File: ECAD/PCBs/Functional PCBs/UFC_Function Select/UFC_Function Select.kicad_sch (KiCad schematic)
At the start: 15 parts

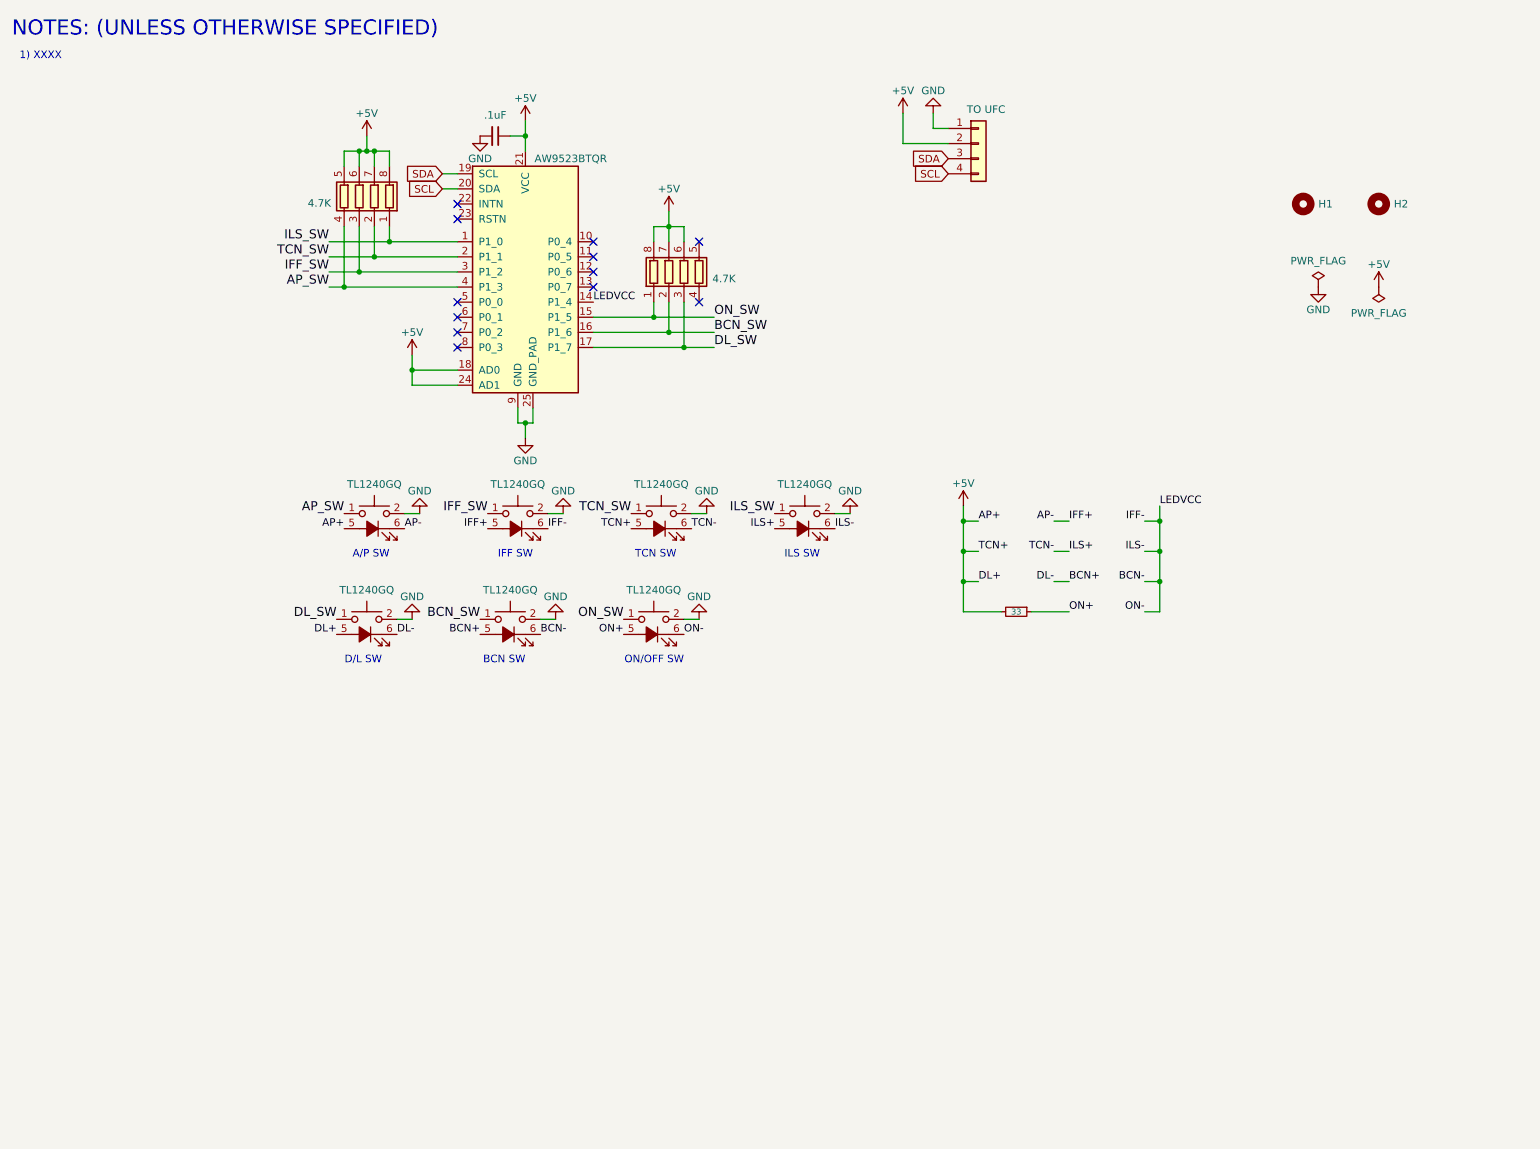
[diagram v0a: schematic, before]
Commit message: ECAD Update
Throttle Controller
-Simplified the solenoid relay circuits
-changed to S2-MINI microcontroller
-Added a second AUX I2C for future ATC connection
-Same mechanical footprint.
UFC v5.5 MAIN and AP KB files (didn't make it last time, oops.)
Added pin sockets 3d model to S2 Mini footprint
Added S2 Mini footprint to the symbol.
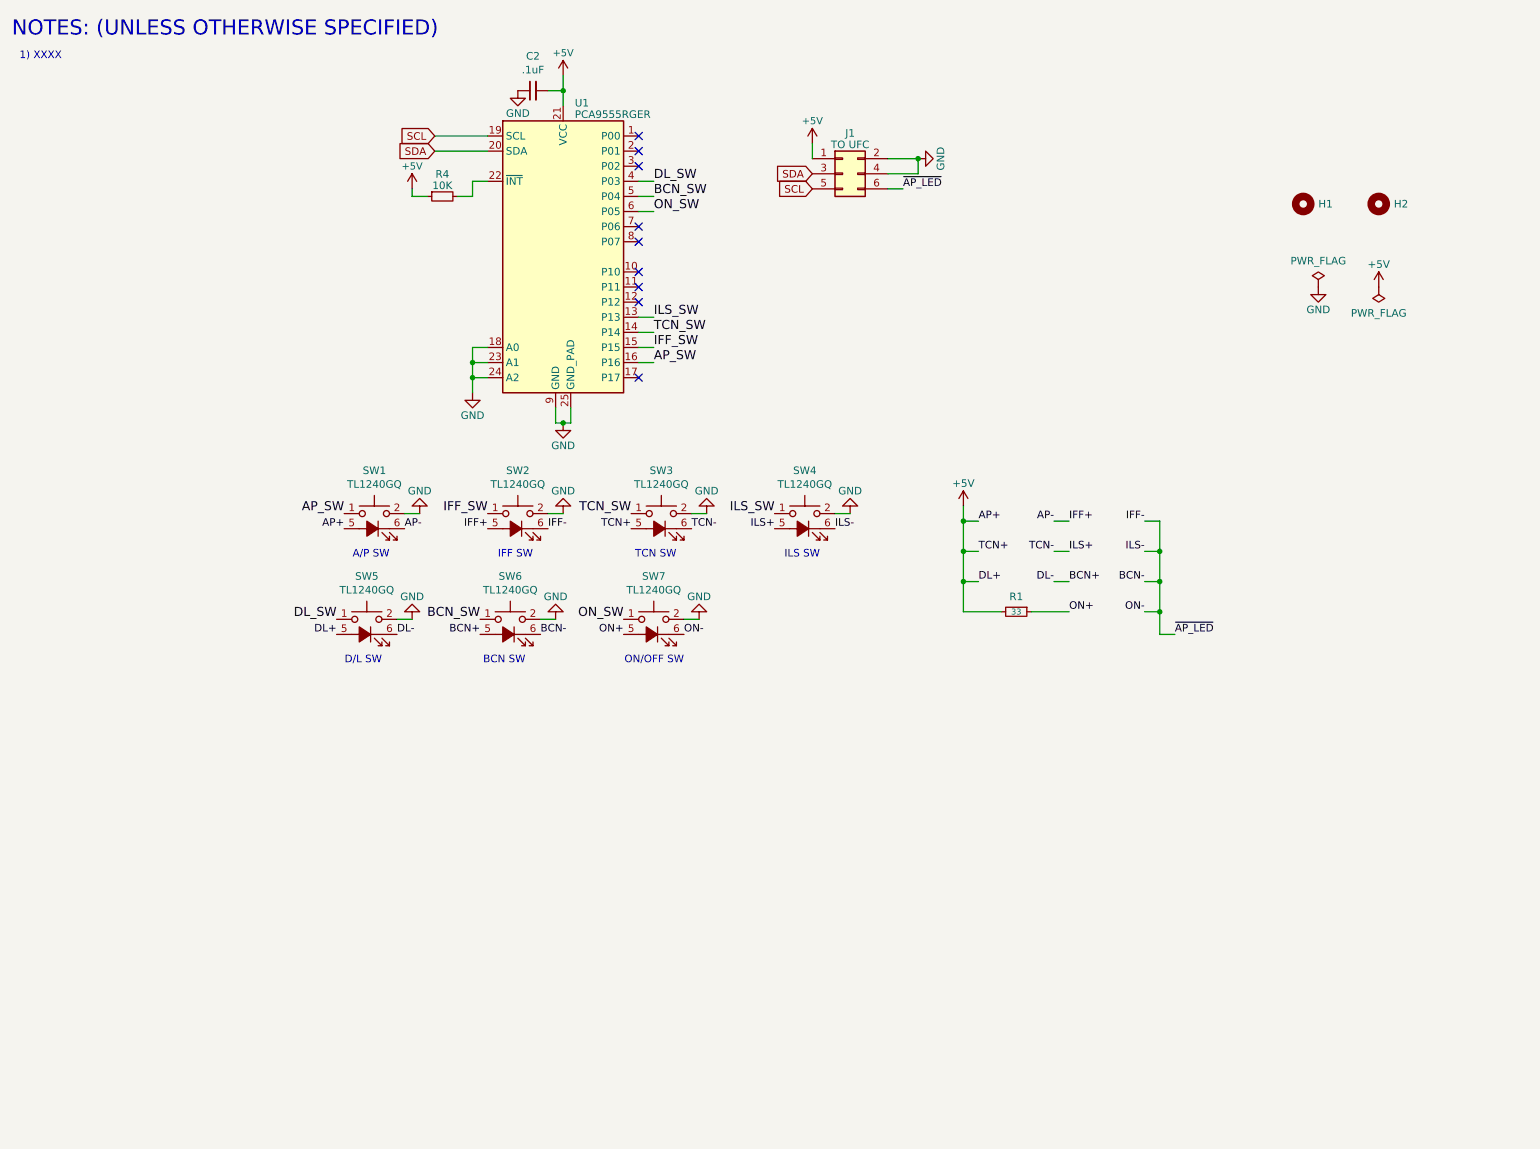
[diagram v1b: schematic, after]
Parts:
- removed ?: TO UFC, Connector_PinHeader_2.54mm:PinHeader_1x04_P2.54mm_Vertical, symbol Connector_Generic:Conn_01x04
- removed ?: AW9523BTQR, Package_DFN_QFN:WQFN-24-1EP_4x4mm_P0.5mm_EP2.6x2.6mm, symbol UFC_Function-Select-rescue:AW9523BTQR-KiCadCustomLib
- removed ?: .1uF, Capacitor_SMD:C_0603_1608Metric, symbol Device:C_Small
- removed ? (x2): 4.7K, Resistor_SMD:R_Array_Convex_4x0603, symbol Device:R_Pack04
- added C2: .1uF, Capacitor_SMD:C_0603_1608Metric, symbol Device:C_Small
- added J1: TO UFC, Connector_PinHeader_2.54mm:PinHeader_2x03_P2.54mm_Vertical, symbol Connector_Generic:Conn_02x03_Odd_Even
- added R4: 10K, Resistor_SMD:R_0603_1608Metric, symbol Device:R_Small
- added U1: PCA9555RGER, Package_DFN_QFN:VQFN-24-1EP_4x4mm_P0.5mm_EP2.45x2.45mm, symbol KiCadCustomLib:PCA9555RGER
- SW1, SW2, SW3, SW4, SW5, SW6, SW7: renamed from ?; footprint KiCAD_Libraries:TL1240GQ -> OH_Footprints:TL1240GQ; symbol UFC_Function-Select-rescue:TL1240GQ-KiCadCustomLib -> KiCadCustomLib:TL1240GQ
- gave numbers to parts that had none: 1
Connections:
- net +5V: now also C2.2, J1.1 (Pin_1), R4.1, U1.21 (VCC)
- net AP_SW: now also U1.16 (P16)
- net BCN-: now also J1.6 (Pin_6)
- net BCN_SW: now also U1.5 (P04)
- net DL_SW: now also U1.4 (P03)
- net GND: now also C2.1, J1.2 (Pin_2), J1.4 (Pin_4), U1.18 (A0), U1.23 (A1), U1.24 (A2), U1.25 (GND_PAD), U1.9 (GND)
- net IFF_SW: now also U1.15 (P15)
- net ILS_SW: now also U1.13 (P13)
- net ON_SW: now also U1.6 (P05)
- net SCL: now also J1.5 (Pin_5), U1.19 (SCL)
- net SDA: now also J1.3 (Pin_3), U1.20 (SDA)
- net TCN_SW: now also U1.14 (P14)
- new net: R4.2, U1.22 (~{INT})
- no-connect marks 12 -> 9

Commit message: Updated Function Select PCB
Replaced tactiles with Omron High-Force Tactiles
Added WS2812B-2020s for Backlighting
Added Interrupt (IRQ) line, replacing the center ground pin on the connector.
Ready for test order.
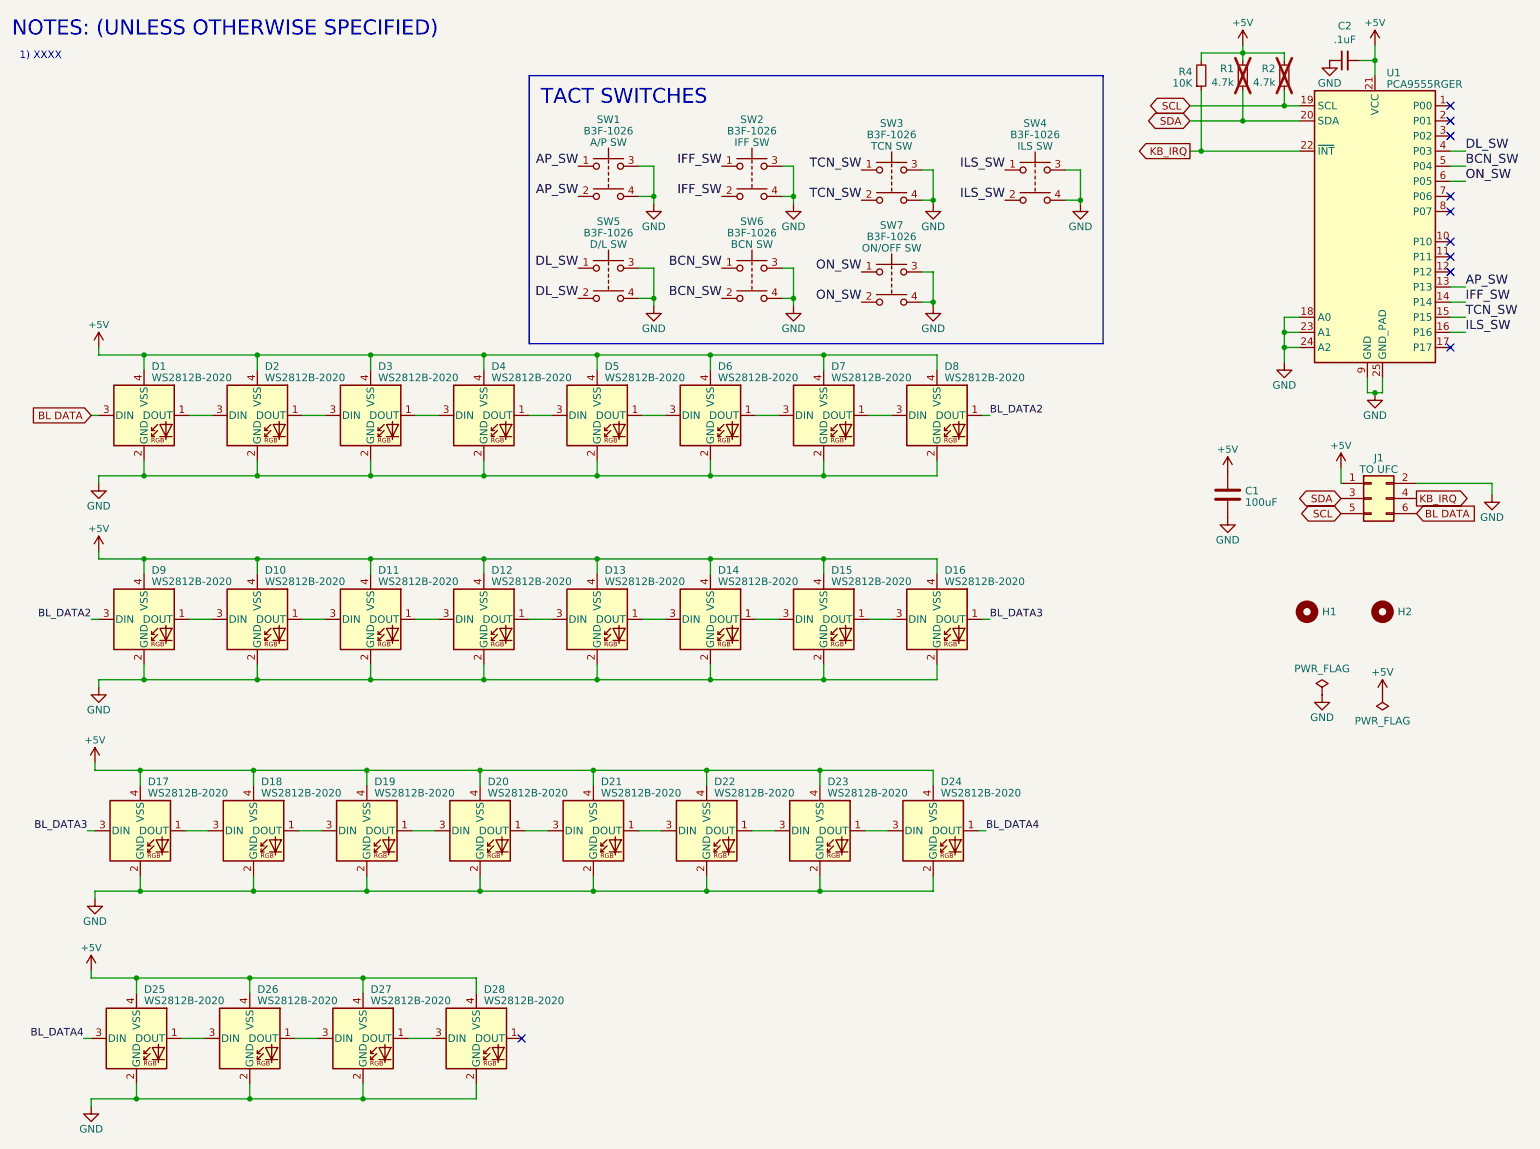
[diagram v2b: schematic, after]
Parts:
- removed SW1, SW2, SW3, SW4, SW5, SW6, SW7: TL1240GQ, OH_Footprints:TL1240GQ, symbol KiCadCustomLib:TL1240GQ
- added C1: 100uF, Capacitor_SMD:CP_Elec_6.3x5.4, symbol Device:C
- added D1, D10, D11, D12, D13, D14, D15, D16, D17, D18, D19, D2, D20, D21, D22, D23, D24, D25, D26, D27, D28, D3, D4, D5, D6, D7, D8, D9: WS2812B-2020, OH_Footprints:LED_WS2812B-2020_PLCC4_2.0x2.0mm, symbol OH_Symbols:WS2812B-2020
- added R2: 4.7k, Resistor_SMD:R_0603_1608Metric, symbol Device:R_Small
- added SW1, SW2, SW3, SW4, SW5, SW6, SW7: B3F-1026, OH_Footprints:Omron_B3F-1026, symbol KiCadCustomLib:Omron_B3F-1026
- H1, H2: footprint MountingHole:MountingHole_3.2mm_M3_DIN965 -> OH_Footprints:MountingHole_3.2mm_M3_DIN965
- R1: value 33 -> 4.7k; footprint Resistor_SMD:R_0402_1005Metric -> Resistor_SMD:R_0603_1608Metric; LCSC C25105 -> C23162; PN 0402WGF330JTCE -> 0603WAF4701T5E; now not fitted
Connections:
- net ON+ is gone; now on net +5V: R1.1
- net +5V: now also R4.2, C1.1, D1.4 (VSS), D10.4 (VSS), D11.4 (VSS), D12.4 (VSS), D13.4 (VSS), D14.4 (VSS), D15.4 (VSS), D16.4 (VSS), D17.4 (VSS), D18.4 (VSS), D19.4 (VSS), D2.4 (VSS), D20.4 (VSS), D21.4 (VSS), D22.4 (VSS), D23.4 (VSS), D24.4 (VSS), D25.4 (VSS), D26.4 (VSS), D27.4 (VSS), D28.4 (VSS), D3.4 (VSS), D4.4 (VSS), D5.4 (VSS), D6.4 (VSS), D7.4 (VSS), D8.4 (VSS), D9.4 (VSS), R2.2; no longer R1.2, R4.1
- net AP_SW: now also U1.13 (P13), SW1.1, SW1.2; no longer U1.16 (P16)
- net BCN_SW: now also SW6.1, SW6.2
- net DL_SW: now also SW5.1, SW5.2
- net GND: now also C1.2, D1.2 (GND), D10.2 (GND), D11.2 (GND), D12.2 (GND), D13.2 (GND), D14.2 (GND), D15.2 (GND), D16.2 (GND), D17.2 (GND), D18.2 (GND), D19.2 (GND), D2.2 (GND), D20.2 (GND), D21.2 (GND), D22.2 (GND), D23.2 (GND), D24.2 (GND), D25.2 (GND), D26.2 (GND), D27.2 (GND), D28.2 (GND), D3.2 (GND), D4.2 (GND), D5.2 (GND), D6.2 (GND), D7.2 (GND), D8.2 (GND), D9.2 (GND), SW1.3, SW1.4, SW2.3, SW2.4, SW3.3, SW3.4, SW4.3, SW4.4, SW5.3, SW5.4, SW6.3, SW6.4, SW7.3, SW7.4; no longer J1.4 (Pin_4)
- net IFF_SW: now also U1.14 (P14), SW2.1, SW2.2; no longer U1.15 (P15)
- net ILS_SW: now also U1.16 (P16), SW4.1, SW4.2; no longer U1.13 (P13)
- net ON_SW: now also SW7.1, SW7.2
- net SCL: now also R2.1
- net SDA: now also R1.2
- net TCN_SW: now also U1.15 (P15), SW3.1, SW3.2; no longer U1.14 (P14)
- net KB_IRQ: now reaches U1.22 (~{INT})
- net KB_IRQ: now also J1.4 (Pin_4), R4.1; no longer R4.2
- net BCN- renamed BL DATA
- net BL DATA: now also D1.3 (DIN)
- new net: D27.1 (DOUT), D28.3 (DIN)
- new net: D26.1 (DOUT), D27.3 (DIN)
- new net: D25.1 (DOUT), D26.3 (DIN)
- new net: D13.1 (DOUT), D14.3 (DIN)
- new net: D12.1 (DOUT), D13.3 (DIN)
- new net: D22.1 (DOUT), D23.3 (DIN)
- new net: D21.1 (DOUT), D22.3 (DIN)
- new net: D2.1 (DOUT), D3.3 (DIN)
- new net: D1.1 (DOUT), D2.3 (DIN)
- new net: D7.1 (DOUT), D8.3 (DIN)
- new net: D3.1 (DOUT), D4.3 (DIN)
- new net: D15.1 (DOUT), D16.3 (DIN)
- new net: D20.1 (DOUT), D21.3 (DIN)
- new net: D19.1 (DOUT), D20.3 (DIN)
- new net: D6.1 (DOUT), D7.3 (DIN)
- new net: D5.1 (DOUT), D6.3 (DIN)
- new net: D11.1 (DOUT), D12.3 (DIN)
- new net: D10.1 (DOUT), D11.3 (DIN)
- new net: D14.1 (DOUT), D15.3 (DIN)
- new net: D4.1 (DOUT), D5.3 (DIN)
- new net: D23.1 (DOUT), D24.3 (DIN)
- new net: D10.3 (DIN), D9.1 (DOUT)
- new net: D18.1 (DOUT), D19.3 (DIN)
- new net: D17.1 (DOUT), D18.3 (DIN)
- new net BL_DATA2: D8.1 (DOUT), D9.3 (DIN)
- new net BL_DATA3: D16.1 (DOUT), D17.3 (DIN)
- new net BL_DATA4: D24.1 (DOUT), D25.3 (DIN)
- no-connect marks 9 -> 10
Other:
- note removed: "A/P SW"
- note removed: "BCN SW"
- note removed: "D/L SW"
- note removed: "IFF SW"
- note removed: "ILS SW"
- note removed: "ON/OFF SW"
- note removed: "TCN SW"
- title: Autopilot Button PCB -> FUNCTION SELECT PCB
- moved on the sheet: C2, H1, H2, J1, R4, U1
